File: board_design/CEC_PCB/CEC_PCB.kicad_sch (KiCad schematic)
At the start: 4 parts, among them J1 HDMI_A, J2 HDMI_A, J3 Conn_01x12_Socket, J4 Conn_01x12_Socket

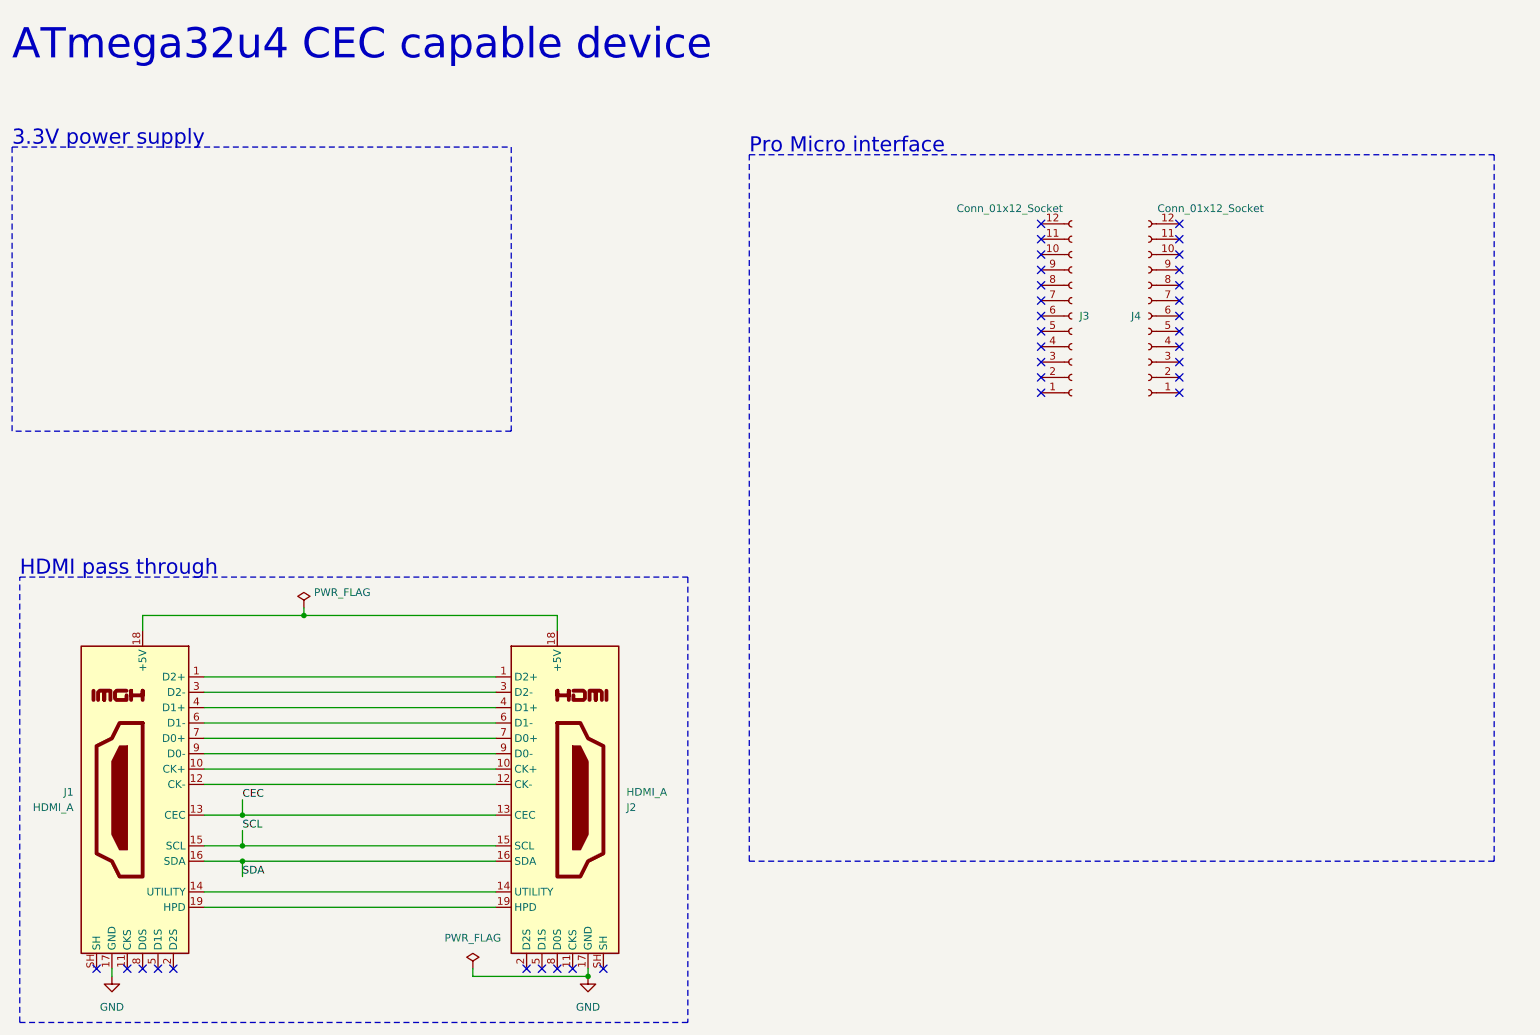
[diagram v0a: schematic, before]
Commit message: LDO for 3.3V power CEC level shifting I2C pull-up resistors
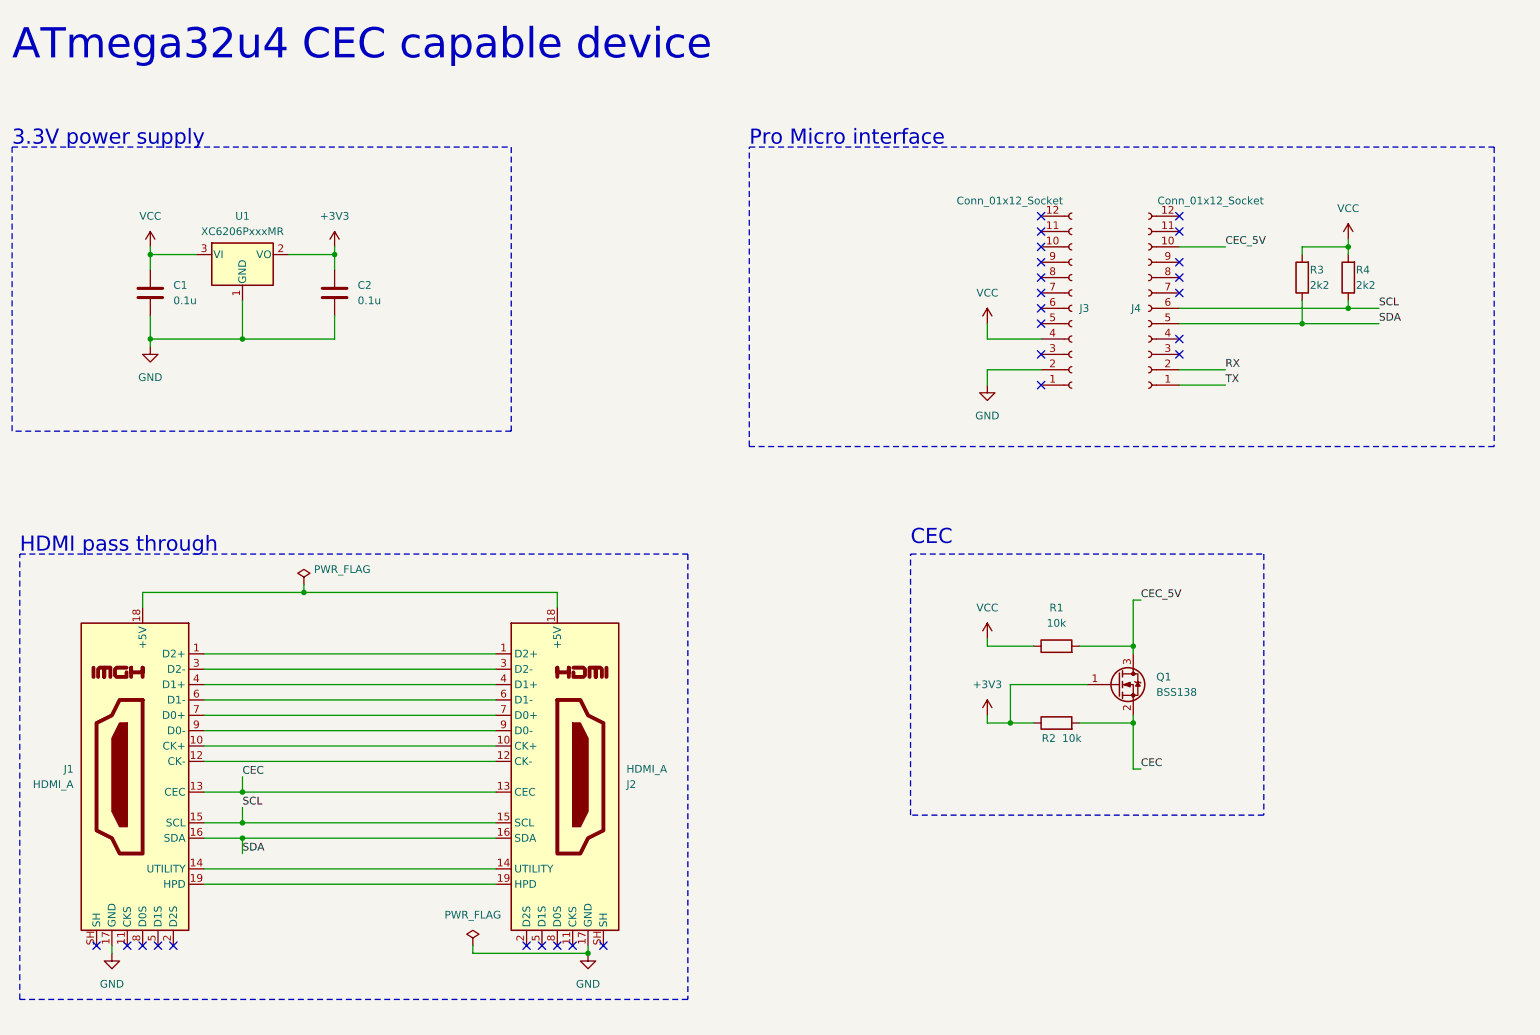
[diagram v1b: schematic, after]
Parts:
- added C1, C2: 0.1u, symbol Device:C
- added Q1: BSS138, Package_TO_SOT_SMD:SOT-23, symbol Transistor_FET:BSS138
- added R1, R2: 10k, symbol Device:R
- added R3, R4: 2k2, symbol Device:R
- added U1: XC6206PxxxMR, Package_TO_SOT_SMD:SOT-23-3, symbol Regulator_Linear:XC6206PxxxMR
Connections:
- net CEC: now also Q1.2 (S), R2.2
- net GND: now also J3.2 (Pin_2), C1.2, C2.2, U1.1 (GND)
- net SCL: now also J4.6 (Pin_6), R4.1
- net SDA: now also J4.5 (Pin_5), R3.1
- net TX: now reaches J4.1 (Pin_1)
- net CEC_5V: now reaches J4.10 (Pin_10)
- net CEC_5V: now also Q1.3 (D), R1.2
- net RX: now reaches J4.2 (Pin_2)
- net VCC: now reaches J3.4 (Pin_4)
- net VCC: now also C1.1, R1.1, R3.2, R4.2, U1.3 (VI)
- new net +3V3: C2.1, Q1.1 (G), R2.1, U1.2 (VO)
- no-connect marks 34 -> 27
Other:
- note added: "CEC"
- moved on the sheet: J1, J2, J3, J4

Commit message: Broke out Pro Micro pins using a connector with two rows Level shifter between CEC pins Mounting holes and debug pins PCB outline defined Crude component placement Copper pours on GND planes
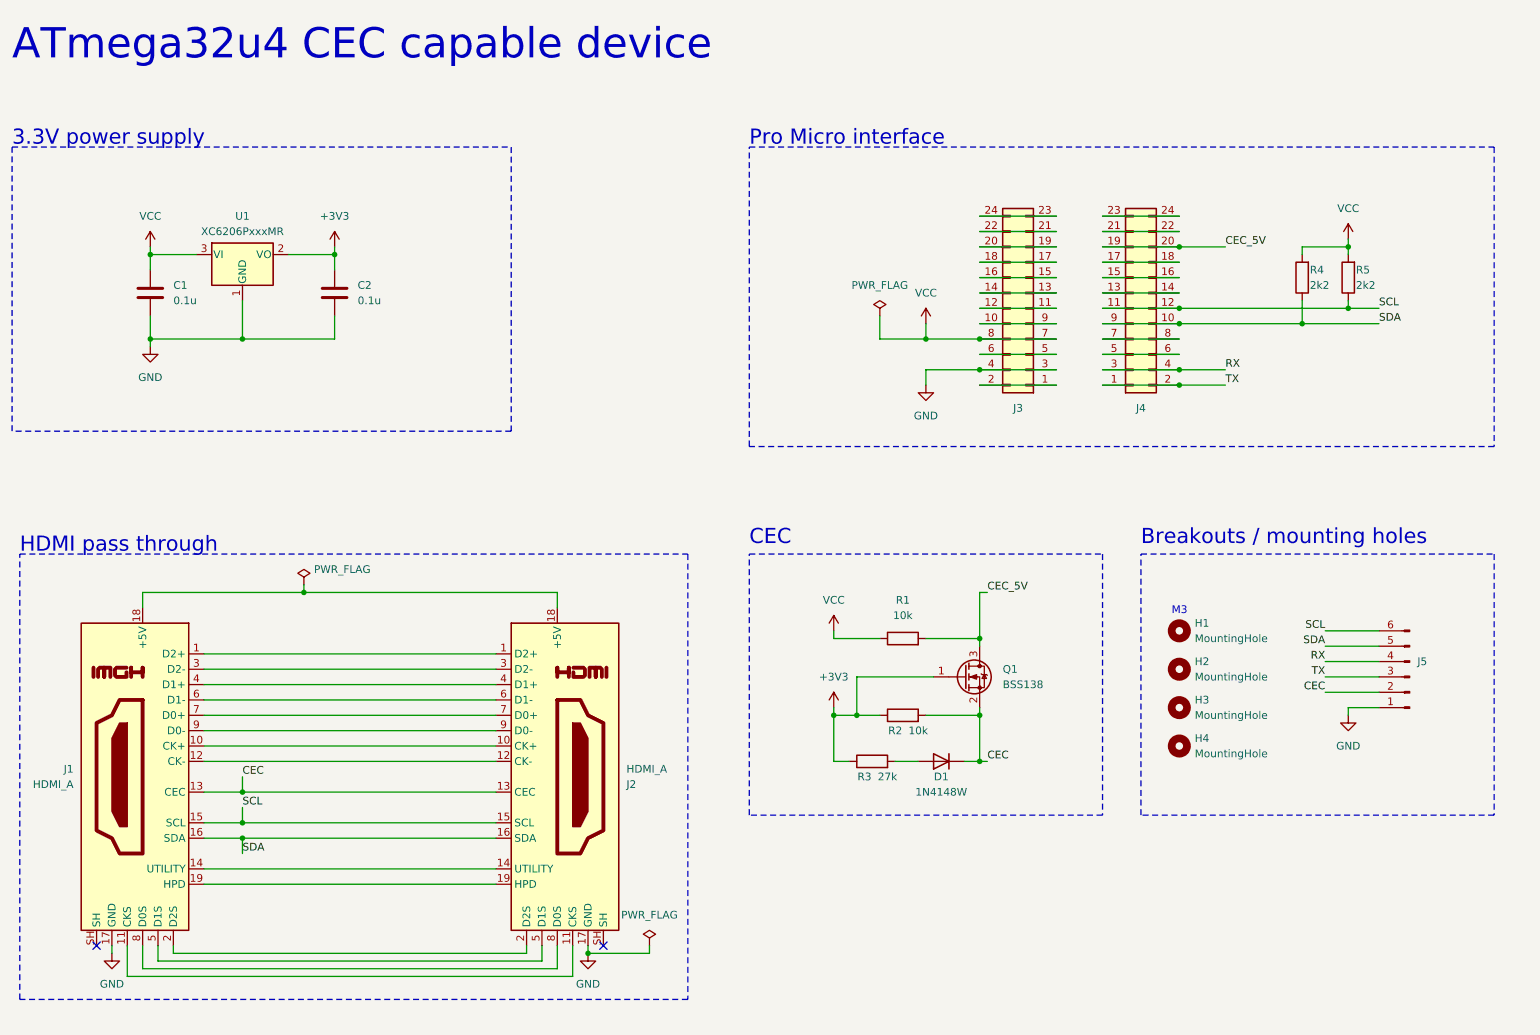
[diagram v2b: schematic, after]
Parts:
- removed J3, J4: Conn_01x12_Socket, Connector_PinSocket_2.54mm:PinSocket_1x12_P2.54mm_Vertical, symbol Connector:Conn_01x12_Socket
- added D1: 1N4148W, Diode_SMD:D_SOD-123, symbol Diode:1N4148W
- added H1, H2, H3, H4: MountingHole, MountingHole:MountingHole_3mm, symbol Mechanical:MountingHole
- added J3, J4: Conn_02x12_Odd_Even, Connector_PinSocket_2.54mm:PinSocket_2x12_P2.54mm_Vertical, symbol Connector_Generic:Conn_02x12_Odd_Even
- added J5: Conn_01x06_Pin, Connector_PinHeader_2.54mm:PinHeader_1x06_P2.54mm_Vertical, symbol Connector:Conn_01x06_Pin
- added R3: 27k, Resistor_SMD:R_0402_1005Metric, symbol Device:R
- C1, C2: footprint (none) -> Capacitor_SMD:C_0402_1005Metric
- R1, R2: footprint (none) -> Resistor_SMD:R_0402_1005Metric
- R4: renamed from R3; footprint (none) -> Resistor_SMD:R_0402_1005Metric
- R5: renamed from R4; footprint (none) -> Resistor_SMD:R_0402_1005Metric
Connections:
- net +3V3: now also R3.1
- net CEC: now also D1.1 (K), J5.2 (Pin_2)
- net CEC_5V: now also J3.19 (Pin_19), J3.20 (Pin_20)
- net GND: now also J4.3 (Pin_3), J4.4 (Pin_4), J5.1 (Pin_1)
- net RX: now also J3.3 (Pin_3), J3.4 (Pin_4), J5.4 (Pin_4)
- net SCL: now also J3.11 (Pin_11), J3.12 (Pin_12), J5.6 (Pin_6)
- net SDA: now also J3.10 (Pin_10), J3.9 (Pin_9), J5.5 (Pin_5)
- net TX: now also J3.1 (Pin_1), J3.2 (Pin_2), J5.3 (Pin_3)
- net VCC: now also J4.7 (Pin_7), J4.8 (Pin_8)
- net at J1.11 (CKS): now also J2.11 (CKS)
- net at J1.2 (D2S): now also J2.2 (D2S)
- net at J1.5 (D1S): now also J2.5 (D1S)
- net at J1.8 (D0S): now also J2.8 (D0S)
- new net: J4.1 (Pin_1), J4.2 (Pin_2)
- new net: J4.10 (Pin_10), J4.9 (Pin_9)
- new net: J4.11 (Pin_11), J4.12 (Pin_12)
- new net: J4.13 (Pin_13), J4.14 (Pin_14)
- new net: J4.15 (Pin_15), J4.16 (Pin_16)
- new net: J4.17 (Pin_17), J4.18 (Pin_18)
- new net: J4.19 (Pin_19), J4.20 (Pin_20)
- new net: J4.21 (Pin_21), J4.22 (Pin_22)
- new net: J4.23 (Pin_23), J4.24 (Pin_24)
- new net: J4.5 (Pin_5), J4.6 (Pin_6)
- new net: D1.2 (A), R3.2
- new net: J3.13 (Pin_13), J3.14 (Pin_14)
- new net: J3.15 (Pin_15), J3.16 (Pin_16)
- new net: J3.17 (Pin_17), J3.18 (Pin_18)
- new net: J3.21 (Pin_21), J3.22 (Pin_22)
- new net: J3.23 (Pin_23), J3.24 (Pin_24)
- new net: J3.5 (Pin_5), J3.6 (Pin_6)
- new net: J3.7 (Pin_7), J3.8 (Pin_8)
- no-connect marks 27 -> 2
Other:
- note added: "Breakouts / mounting holes"
- note added: "M3"
- moved on the sheet: Q1, R1, R2

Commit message: Labels for nets in the schematic Board size change Parts placement change Basic routing
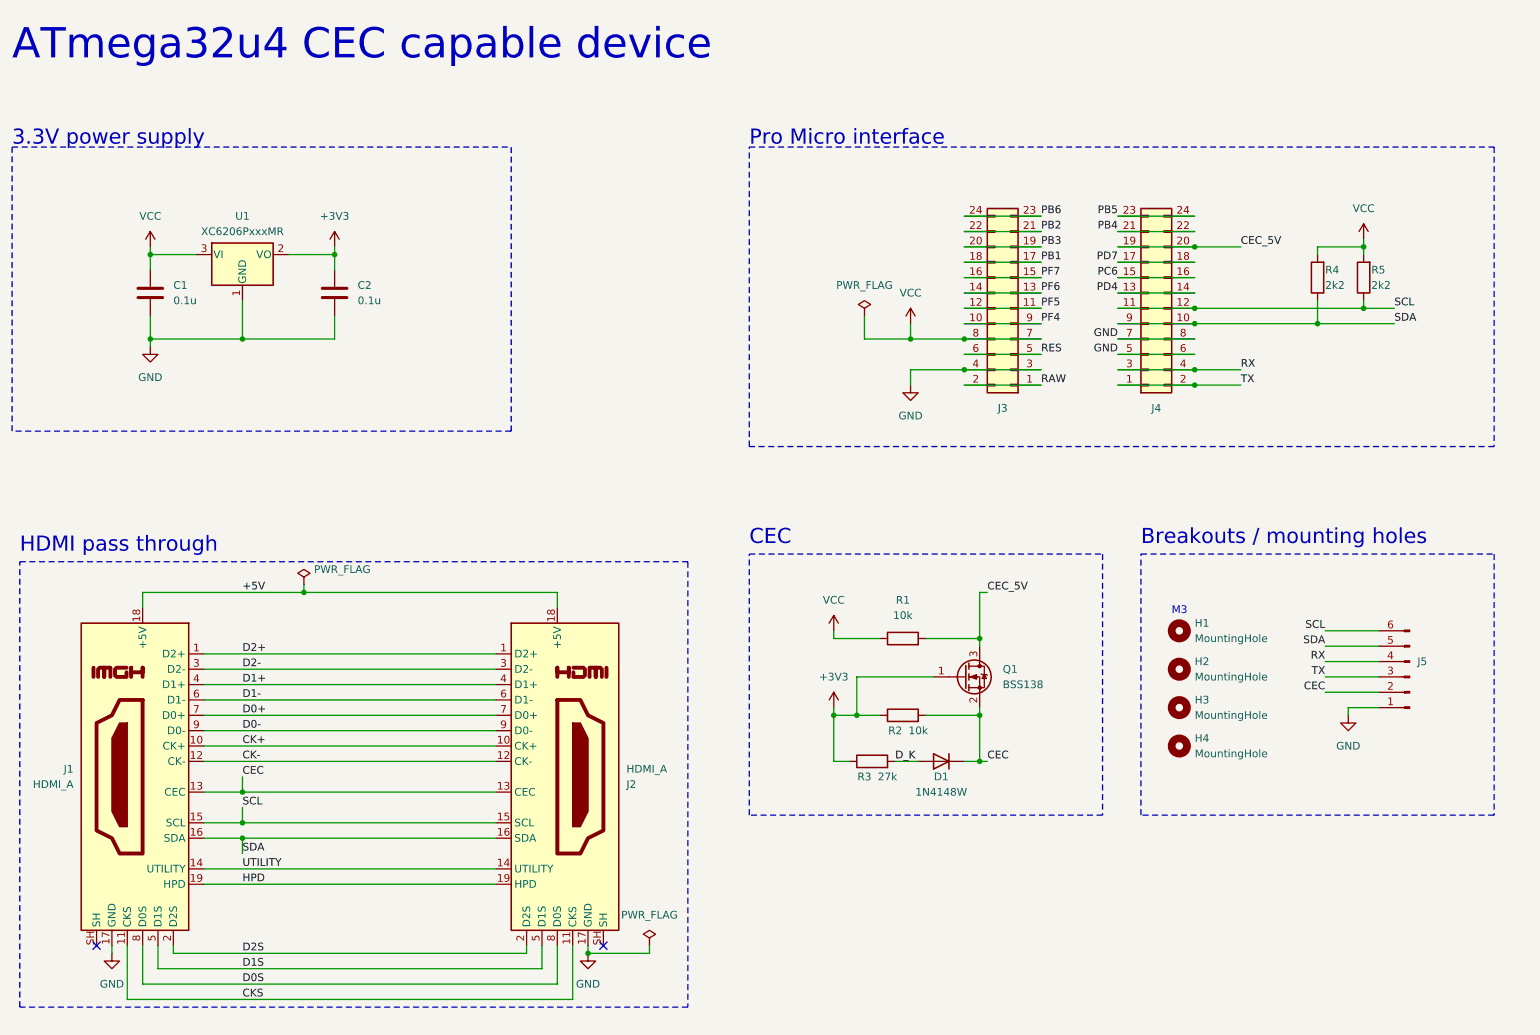
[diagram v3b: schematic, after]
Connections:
- net GND: now also J3.5 (Pin_5), J3.6 (Pin_6), J3.7 (Pin_7), J3.8 (Pin_8)
- net D2+: now reaches J1.1 (D2+), J2.1 (D2+)
- net CK+: now reaches J1.10 (CK+), J2.10 (CK+)
- net CKS: now reaches J1.11 (CKS), J2.11 (CKS)
- net CK-: now reaches J1.12 (CK-), J2.12 (CK-)
- net UTILITY: now reaches J1.14 (UTILITY), J2.14 (UTILITY)
- net +5V: now reaches J1.18 (+5V), J2.18 (+5V)
- net HPD: now reaches J1.19 (HPD), J2.19 (HPD)
- net D2S: now reaches J1.2 (D2S), J2.2 (D2S)
- net D2-: now reaches J1.3 (D2-), J2.3 (D2-)
- net D1+: now reaches J1.4 (D1+), J2.4 (D1+)
- net D1S: now reaches J1.5 (D1S), J2.5 (D1S)
- net D1-: now reaches J1.6 (D1-), J2.6 (D1-)
- net D0+: now reaches J1.7 (D0+), J2.7 (D0+)
- net D0S: now reaches J1.8 (D0S), J2.8 (D0S)
- net D0-: now reaches J1.9 (D0-), J2.9 (D0-)
- net RAW: now reaches J4.1 (Pin_1), J4.2 (Pin_2)
- net PF4: now reaches J4.10 (Pin_10), J4.9 (Pin_9)
- net PF5: now reaches J4.11 (Pin_11), J4.12 (Pin_12)
- net PF6: now reaches J4.13 (Pin_13), J4.14 (Pin_14)
- net PF7: now reaches J4.15 (Pin_15), J4.16 (Pin_16)
- net PB1: now reaches J4.17 (Pin_17), J4.18 (Pin_18)
- net PB3: now reaches J4.19 (Pin_19), J4.20 (Pin_20)
- net PB2: now reaches J4.21 (Pin_21), J4.22 (Pin_22)
- net PB6: now reaches J4.23 (Pin_23), J4.24 (Pin_24)
- net RES: now reaches J4.5 (Pin_5), J4.6 (Pin_6)
- net D_K: now reaches D1.2 (A), R3.2
- net PD4: now reaches J3.13 (Pin_13), J3.14 (Pin_14)
- net PC6: now reaches J3.15 (Pin_15), J3.16 (Pin_16)
- net PD7: now reaches J3.17 (Pin_17), J3.18 (Pin_18)
- net PB4: now reaches J3.21 (Pin_21), J3.22 (Pin_22)
- net PB5: now reaches J3.23 (Pin_23), J3.24 (Pin_24)
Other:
- moved on the sheet: J3, J4, R4, R5

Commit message: Changed VDO capacitors to 1uF Some routing changes Ground vias throughout the PCB Some optimizations
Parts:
- C1, C2: value 0.1u -> 1u
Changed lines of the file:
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@@
       (effects (font (size 1.27 1.27)) (justify left))
     )
-    (property "Value" "0.1u" (at 54.61 66.04 0)
+    (property "Value" "1u" (at 54.61 66.04 0)
       (effects (font (size 1.27 1.27)) (justify left))
     )
@@
       (effects (font (size 1.27 1.27)) (justify left))
     )
-    (property "Value" "0.1u" (at 85.09 66.04 0)
+    (property "Value" "1u" (at 85.09 66.04 0)
       (effects (font (size 1.27 1.27)) (justify left))
     )
